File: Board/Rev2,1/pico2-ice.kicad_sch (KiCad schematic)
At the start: 122 parts, among them J1 USB_C_Receptacle_USB2.0, J2 Conn_02x20_Odd_Even, J3 Conn_02x20_Odd_Even, J5 BM03B-SRSS-TB, J6 SFV22R-2STE1HLF, SW1 CS1213AGF260, SW2 CS1213AGF260, U1 NCP115AMX120TCG, U2 W25Q32JVSSIQ, U3 RP2350_80QFN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

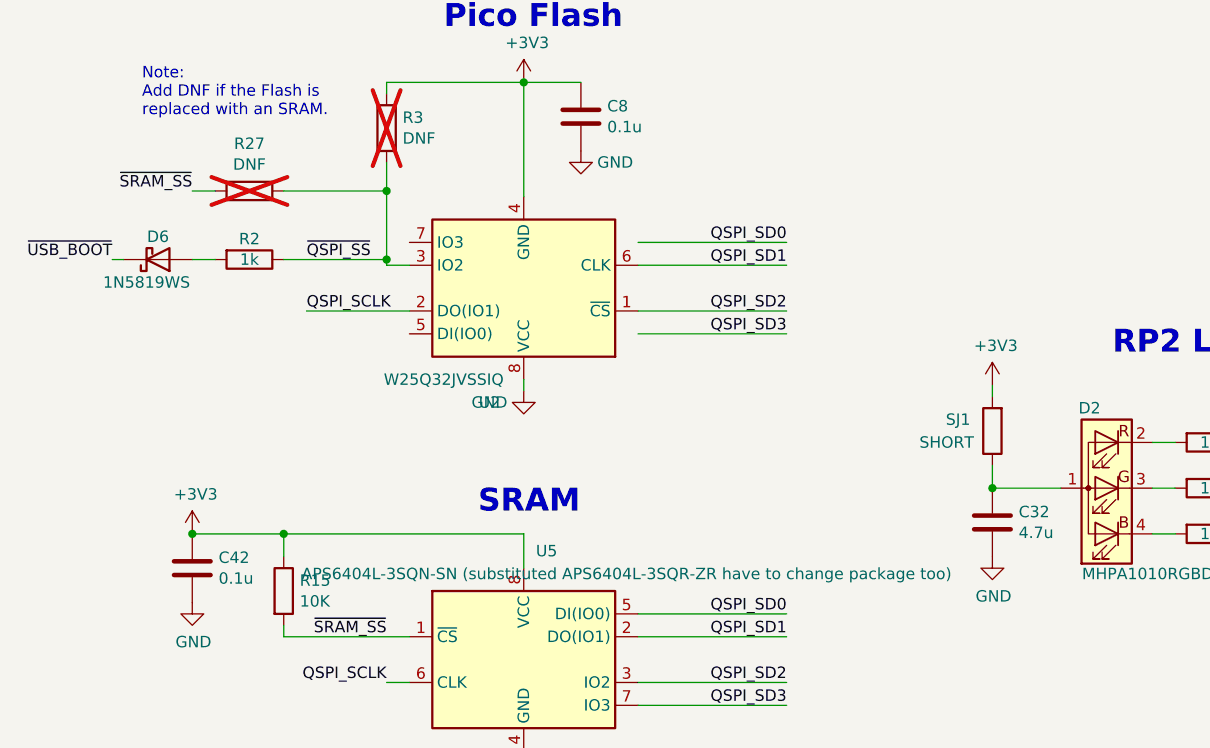
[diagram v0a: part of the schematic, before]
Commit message: Fixed U2 getting flipped on schematic
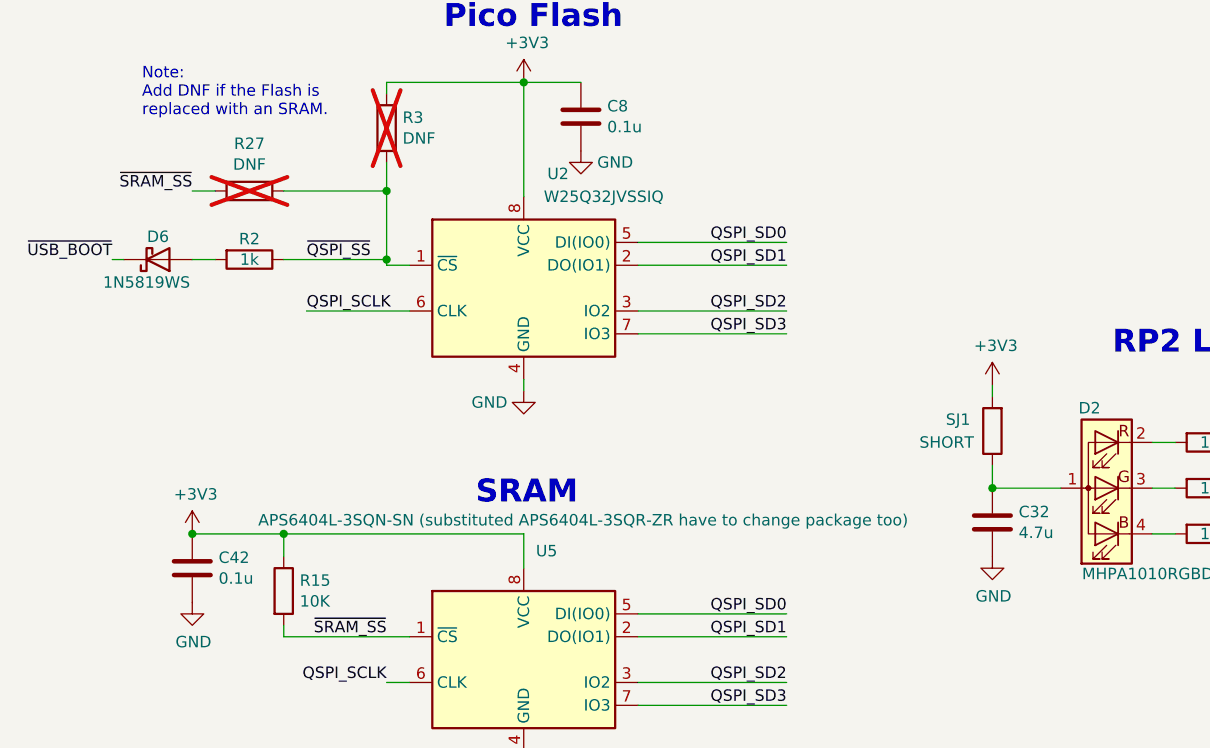
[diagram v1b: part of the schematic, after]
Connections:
- net +3V3: now also U2.8 (VCC); no longer U2.4 (GND)
- net GND: now also U2.4 (GND); no longer U2.8 (VCC)
- net QSPI_SCLK: now also U2.6 (CLK); no longer U2.2 (DO(IO1))
- net QSPI_SD0: now also U2.5 (DI(IO0))
- net QSPI_SD1: now also U2.2 (DO(IO1)); no longer U2.6 (CLK)
- net QSPI_SD2: now also U2.3 (IO2); no longer U2.1 (~{CS})
- net QSPI_SD3: now also U2.7 (IO3)
- net ~{QSPI_SS}: now also U2.1 (~{CS}); no longer U2.3 (IO2)
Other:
- moved on the sheet: U2
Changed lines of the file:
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@@
 	(text "SRAM"
 		(exclude_from_sim no)
-		(at 66.04 375.158 0)
+		(at 65.786 374.142 0)
 		(effects
 			(font
@@
 		)
 		(property "Value" "APS6404L-3SQN-SN (substituted  APS6404L-3SQR-ZR have to change package too)"
-			(at 82.55 381.635 0)
+			(at 77.724 375.666 0)
 			(effects
 				(font
@@
 	(symbol
 		(lib_id "UPduino_v3.0:W25Q32JVSS-Memory_Flash")
-		(at 71.12 349.885 180)
+		(at 71.12 349.885 0)
 		(unit 1)
 		(exclude_from_sim no)
@@
 		(dnp no)
 		(property "Reference" "U2"
-			(at 67.31 362.585 0)
+			(at 74.93 337.185 0)
 			(effects
 				(font
@@
 		)
 		(property "Value" "W25Q32JVSSIQ"
-			(at 62.23 360.045 0)
+			(at 80.01 339.725 0)
 			(effects
 				(font
